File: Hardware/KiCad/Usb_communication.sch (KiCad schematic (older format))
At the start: 23 parts, among them P1 CONN_01X03, P10 CONN_01X03, P11 CONN_01X03, P12 CONN_01X03, P13 CONN_01X03, P14 CONN_01X03, P15 CONN_01X03, P16 CONN_01X03, P17 CONN_01X03, P18 CONN_01X03, P19 CONN_01X03, P2 CONN_01X03, P20 CONN_01X03, P21 CONN_01X03, P22 CONN_01X03, P23 I2C, P3 CONN_01X03, P4 CONN_01X03, P5 CONN_01X03, P6 CONN_01X03, P7 CONN_01X03, P8 CONN_01X03, P9 CONN_01X03

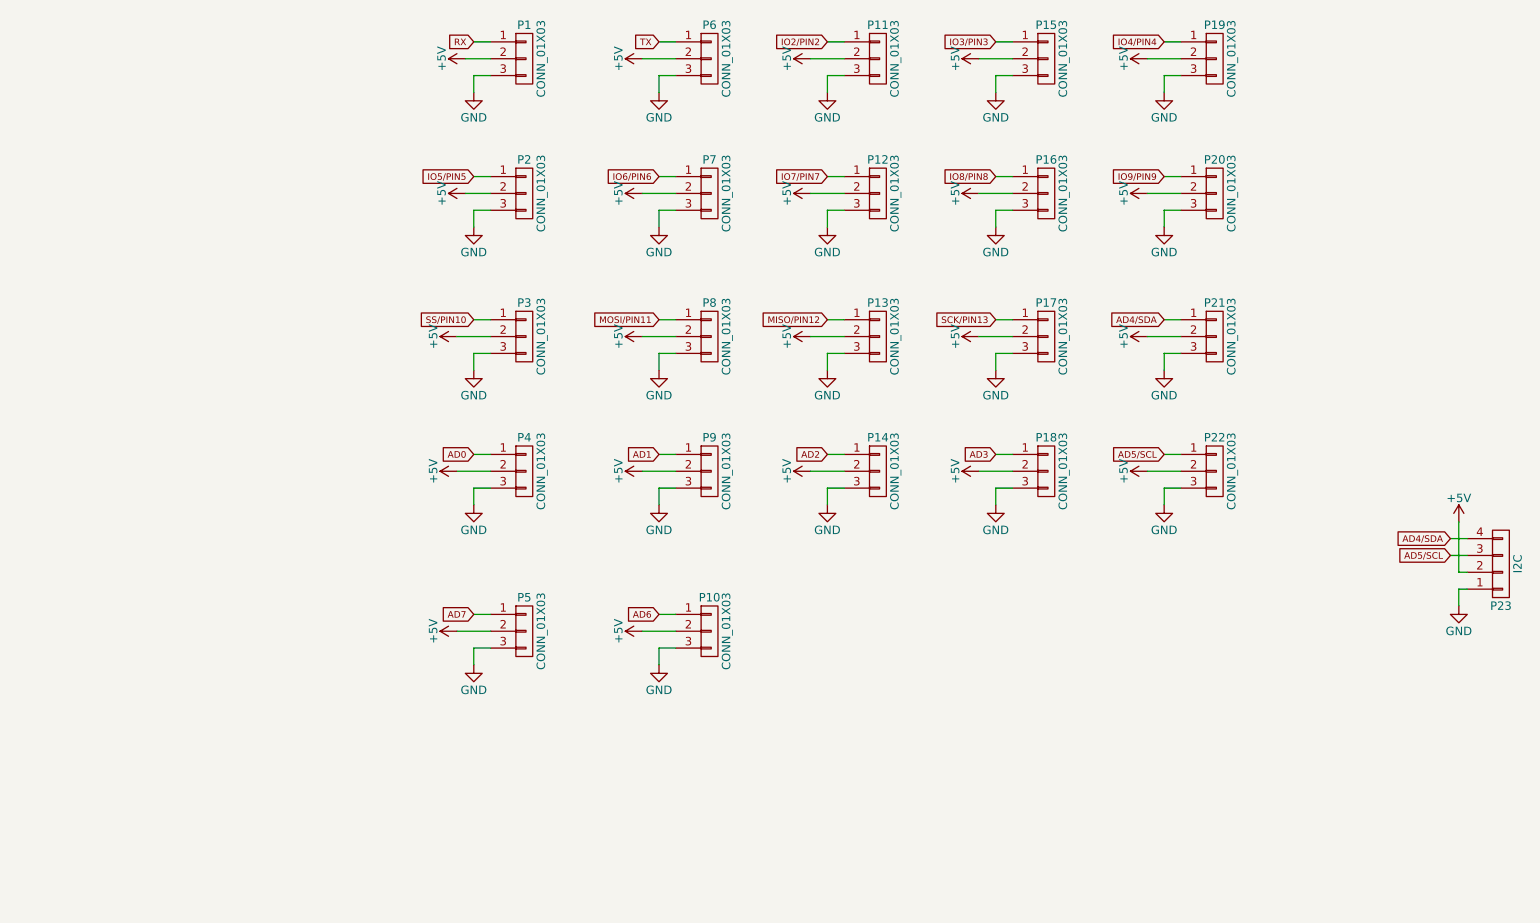
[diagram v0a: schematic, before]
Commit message: Cambiando el árbol de carpetas
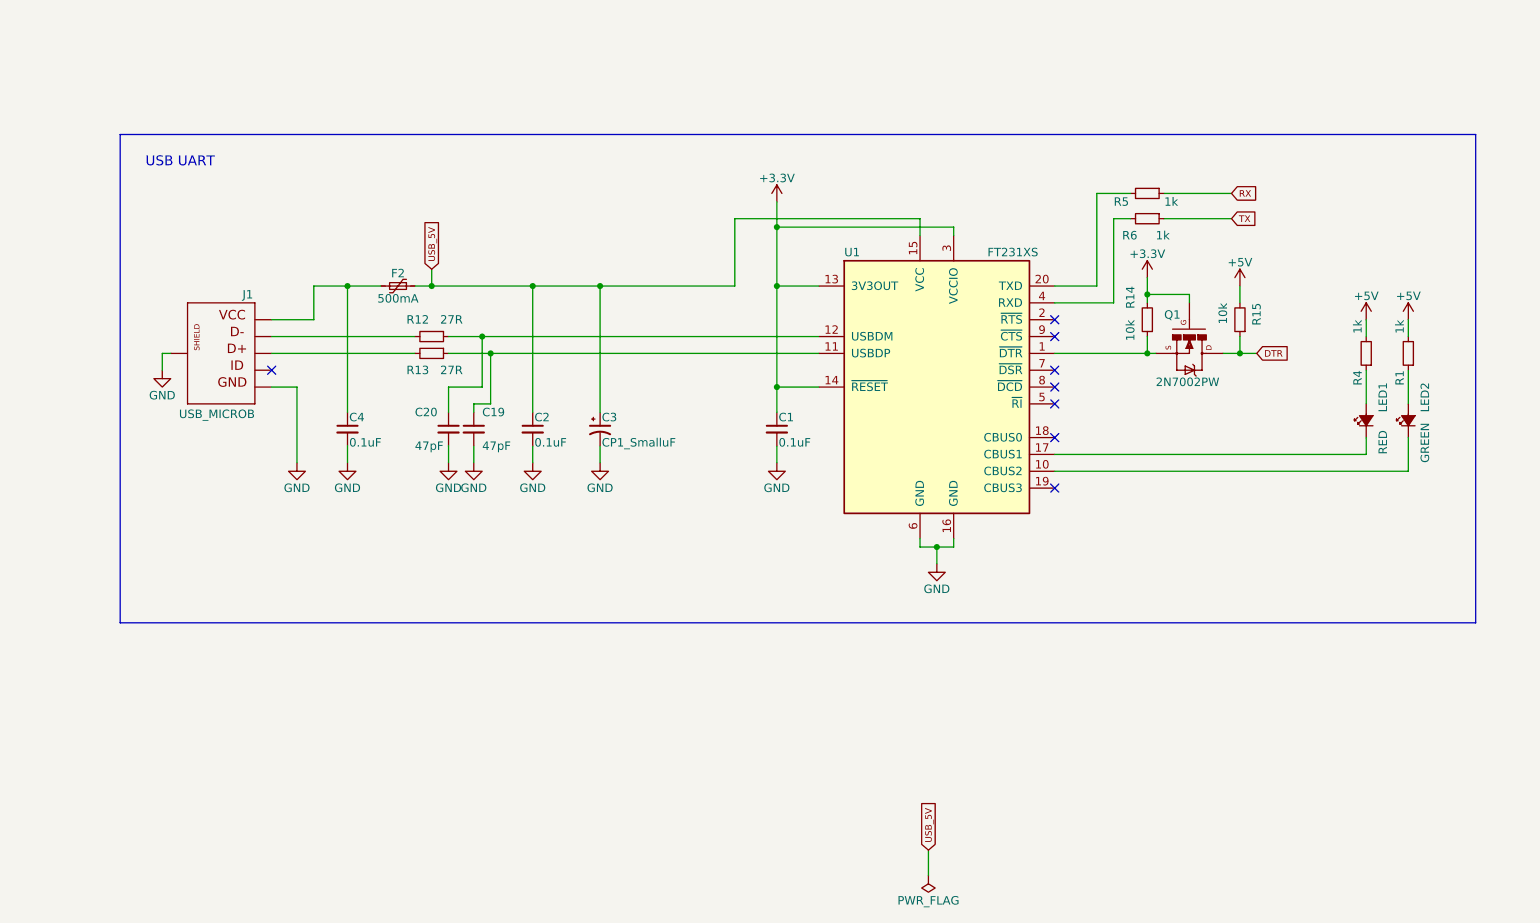
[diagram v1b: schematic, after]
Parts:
- removed P1, P10, P11, P12, P13, P14, P15, P16, P17, P18, P19, P2, P20, P21, P22, P3, P4, P5, P6, P7, P8, P9: CONN_01X03, Pin_Headers:Pin_Header_Straight_1x03_Pitch2.54mm, symbol CONN_01X03
- removed P23: I2C, Connectors_JST:JST_PH_S4B-PH-K_04x2.00mm_Angled, symbol CONN_01X04
- added C1, C2, C4: 0.1uF, lib_sch:C_0805, symbol C_Small
- added C19, C20: 47pF, lib_sch:C_0805, symbol C_Small
- added C3: CP1_SmalluF, lib_sch:CP_Tantalum_Case-A_EIA-3216-18_Reflow, symbol CP1_Small
- added F2: 500mA, lib_sch:R_1812, symbol Polyfuse_Small
- added J1: USB_MICROB, lib_sch:USB_Micro-B_Molex-105017-0001, symbol USB_MICROB_PLUGCONN-11752
- added LED1: RED, lib_sch:LED_0805, symbol LED_Small_ALT
- added LED2: GREEN, lib_sch:LED_0805, symbol LED_Small_ALT
- added Q1: 2N7002PW, lib_sch:SOT-323_SC-70, symbol MOSFET-NCHANNEL2N7002PW
- added R1, R4, R5, R6: 1k, lib_sch:R_0805, symbol R_Small
- added R12, R13: 27R, lib_sch:R_0805, symbol R_Small
- added R14, R15: 10k, lib_sch:R_0805, symbol R_Small
- added U1: FT231XS, lib_sch:SSOP-20, symbol FT231XS
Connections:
- net +5V: now also R1.2, R15.2, R4.2
- net GND: now also C1.2, C19.2, C2.2, C20.2, C3.2, C4.2, J1.5 (GND), J1.6 (SHIELD), U1.16 (GND), U1.6 (GND)
- net RX: now also R5.1
- net TX: now also R6.1
- new net: Q1.2 (S), R14.1, U1.1 (~DTR)
- new net: C4.1, F2.2, J1.1 (VCC)
- new net: C20.1, R12.1, U1.12 (USBDM)
- new net: J1.2 (D-), R12.2
- new net: LED1.1 (K), U1.17 (CBUS1)
- new net: LED1.2 (A), R4.1
- new net: J1.3 (D+), R13.2
- new net: LED2.1 (K), U1.10 (CBUS2)
- new net: C19.1, R13.1, U1.11 (USBDP)
- new net: R5.2, U1.20 (TXD)
- new net: R6.2, U1.4 (RXD)
- new net: LED2.2 (A), R1.1
- new net +3V3: C1.1, Q1.1 (G), R14.2, U1.13 (3V3OUT), U1.14 (~RESET), U1.3 (VCCIO)
- new net DTR: Q1.3 (D), R15.1
- new net USB_5V: C2.1, C3.1, F2.1, U1.15 (VCC)
- no-connect marks 0 -> 8
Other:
- note added: "USB UART\n"

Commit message: Valores cambiados
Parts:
- C1, C2, C4: value 0.1uF -> 100nF
- C3: value CP1_SmalluF -> 10nF

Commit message: preparando archivos
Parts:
- C1, C19, C2, C20, C4: symbol C_Small -> Grape:C_Small
- C3: symbol CP1_Small -> Grape:CP1_Small
- F2: symbol Polyfuse_Small -> Grape:Polyfuse_Small
- J1: symbol USB_MICROB_PLUGCONN-11752 -> Grape:USB_MICROB_PLUGCONN-11752
- LED1, LED2: symbol LED_Small_ALT -> Grape:LED_Small_ALT
- Q1: symbol MOSFET-NCHANNEL2N7002PW -> Grape:MOSFET-NCHANNEL2N7002PW
- R1, R12, R13, R14, R15, R4, R5, R6: symbol R_Small -> Grape:R_Small
- U1: symbol FT231XS -> Grape:FT231XS
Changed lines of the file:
@@
-EESchema Schematic File Version 2
-LIBS:Grape
-EELAYER 25 0
+EESchema Schematic File Version 4
+LIBS:Grape-cache
+EELAYER 26 0
 EELAYER END
 $Descr A4 11693 8268
@@
 $EndDescr
 $Comp
-L MOSFET-NCHANNEL2N7002PW Q1
+L Grape:MOSFET-NCHANNEL2N7002PW Q1
 U 1 1 5A5B8C16
 P 8050 3850
@@
 $EndComp
 $Comp
-L Polyfuse_Small F2
+L Grape:Polyfuse_Small F2
 U 1 1 5A5B942E
 P 3350 3450
@@
 $EndComp
 $Comp
-L R_Small R12
+L Grape:R_Small R12
 U 1 1 5A5B9487
 P 3550 3750
@@
 $EndComp
 $Comp
-L CP1_Small C3
+L Grape:CP1_Small C3
 U 1 1 5A5B962D
 P 4550 4300
@@
 $EndComp
 $Comp
-L LED_Small_ALT LED1
+L Grape:LED_Small_ALT LED1
 U 1 1 5A5B9670
 P 9100 4250
@@
 $EndComp
 $Comp
-L USB_MICROB_PLUGCONN-11752 J1
+L Grape:USB_MICROB_PLUGCONN-11752 J1
 U 1 1 5A5B97D7
 P 2300 3850
@@
 $EndComp
 $Comp
-L FT231XS U1
+L Grape:FT231XS U1
 U 1 1 5A5B991A
 P 6550 4050
@@
 $EndComp
 $Comp
-L GND #PWR01
+L Grape:GND #PWR01
 U 1 1 5A5B9BEF
 P 2750 4500
@@
 $EndComp
 $Comp
-L GND #PWR02
+L Grape:GND #PWR02
 U 1 1 5A5B9C19
 P 1950 3950
@@
 $EndComp
 $Comp
-L C_Small C4
+L Grape:C_Small C4
 U 1 1 5A5B9CAA
 P 3050 4300
@@
 $EndComp
 $Comp
-L GND #PWR03
+L Grape:GND #PWR03
 U 1 1 5A5B9DDB
 P 3050 4500
@@
 $EndComp
 $Comp
-L R_Small R13
+L Grape:R_Small R13
 U 1 1 5A5BA086
 P 3550 3850
@@
 NoConn ~ 2600 3950
 $Comp
-L C_Small C20
+L Grape:C_Small C20
 U 1 1 5A5BA37A
 P 3650 4300
@@
 $EndComp
 $Comp
-L C_Small C19
+L Grape:C_Small C19
 U 1 1 5A5BA405
 P 3800 4300
@@
 $EndComp
 $Comp
-L GND #PWR04
+L Grape:GND #PWR04
 U 1 1 5A5BA69F
 P 3650 4500
@@
 $EndComp
 $Comp
-L GND #PWR05
+L Grape:GND #PWR05
 U 1 1 5A5BA6CE
 P 3800 4500
@@
 $EndComp
 $Comp
-L C_Small C2
+L Grape:C_Small C2
 U 1 1 5A5BAC9D
 P 4150 4300
@@
 $EndComp
 $Comp
-L GND #PWR06
+L Grape:GND #PWR06
 U 1 1 5A5BAD72
 P 4150 4500
@@
 $EndComp
 $Comp
-L GND #PWR07
+L Grape:GND #PWR07
 U 1 1 5A5BB0A6
 P 4550 4500
@@
 	2850 3650 2850 3450
 Wire Wire Line
-	2850 3450 3250 3450
+	2850 3450 3050 3450
 Wire Wire Line
 	3050 4200 3050 3450
@@
 	3850 4050 3850 3750
 Wire Wire Line
-	3650 3750 5850 3750
-Wire Wire Line
-	3650 3850 5850 3850
+	3650 3750 3850 3750
+Wire Wire Line
+	3650 3850 3900 3850
 Wire Wire Line
 	3900 3850 3900 4150
@@
 	4150 3450 4150 4200
 Wire Wire Line
-	3450 3450 5350 3450
+	3450 3450 3550 3450
 Wire Wire Line
 	3550 3450 3550 3350
@@
 Connection ~ 4550 3450
 $Comp
-L C_Small C1
+L Grape:C_Small C1
 U 1 1 5A5BB3AE
 P 5600 4300
@@
 $EndComp
 $Comp
-L GND #PWR08
+L Grape:GND #PWR08
 U 1 1 5A5BB45B
 P 5600 4500
@@
 	5600 4400 5600 4500
 Wire Wire Line
-	5600 2950 5600 4200
+	5600 2950 5600 3100
 Wire Wire Line
 	5600 4050 5850 4050
@@
 Connection ~ 5600 3100
 $Comp
-L +3.3V #PWR09
+L Grape:+3.3V #PWR09
 U 1 1 5A5BB5E3
 P 5600 2950
@@
 $EndComp
 $Comp
-L GND #PWR010
+L Grape:GND #PWR010
 U 1 1 5A5BB73F
 P 6550 5100
@@
 	6450 4950 6450 5000
 Wire Wire Line
-	6450 5000 6650 5000
+	6450 5000 6550 5000
 Wire Wire Line
 	6550 5000 6550 5100
@@
 NoConn ~ 7250 4150
 $Comp
-L R_Small R5
+L Grape:R_Small R5
 U 1 1 5A5BBBAB
 P 7800 2900
@@
 $EndComp
 $Comp
-L R_Small R6
+L Grape:R_Small R6
 U 1 1 5A5BBD20
 P 7800 3050
@@
 TX
 $Comp
-L LED_Small_ALT LED2
+L Grape:LED_Small_ALT LED2
 U 1 1 5A5BC688
 P 9350 4250
@@
 	9350 4550 7250 4550
 $Comp
-L R_Small R4
+L Grape:R_Small R4
 U 1 1 5A5BC7D4
 P 9100 3850
@@
 $EndComp
 $Comp
-L R_Small R1
+L Grape:R_Small R1
 U 1 1 5A5BC864
 P 9350 3850
@@
 	9350 3950 9350 4150
 $Comp
-L +5V #PWR011
+L Grape:+5V #PWR011
 U 1 1 5A5BCDBB
 P 9100 3650
@@
 $EndComp
 $Comp
-L +5V #PWR012
+L Grape:+5V #PWR012
 U 1 1 5A5BCE2C
 P 9350 3650
@@
 	9100 3650 9100 3750
 Wire Wire Line
-	7250 3850 7850 3850
-$Comp
-L R_Small R14
+	7250 3850 7800 3850
+$Comp
+L Grape:R_Small R14
 U 1 1 5A5BD495
 P 7800 3650
@@
 $EndComp
 $Comp
-L R_Small R15
+L Grape:R_Small R15
 U 1 1 5A5BD4FF
 P 8350 3650
@@
 Connection ~ 7800 3850
 Wire Wire Line
-	8250 3850 8450 3850
+	8250 3850 8350 3850
 Wire Wire Line
 	8350 3850 8350 3750
 Connection ~ 8350 3850
 $Comp
-L +5V #PWR013
+L Grape:+5V #PWR013
 U 1 1 5A5BD7FA
 P 8350 3450
@@
 	8350 3450 8350 3550
 $Comp
-L +3.3V #PWR014
+L Grape:+3.3V #PWR014
 U 1 1 5A5BDBB8
 P 7800 3400
@@
 $EndComp
 Wire Wire Line
-	7800 3400 7800 3550
+	7800 3400 7800 3500
 Wire Wire Line
 	7800 3500 8050 3500
@@
 $Bitmap
 Pos 10850 6200
-Scale 0,950000
+Scale 0.000000
 Data
 89 50 4E 47 0D 0A 1A 0A 00 00 00 0D 49 48 44 52 00 00 00 C1 00 00 00 8F 08 06 00 00 00 43 10 BF
@@
 $Bitmap
 Pos 7250 6700
-Scale 0,950000
+Scale 0.000000
 Data
 89 50 4E 47 0D 0A 1A 0A 00 00 00 0D 49 48 44 52 00 00 00 91 00 00 00 36 08 06 00 00 00 C7 C1 7B
@@
 USB_5V
 $Comp
-L PWR_FLAG #FLG015
+L Grape:PWR_FLAG #FLG015
 U 1 1 5A5DCFF9
 P 6500 6950
@@
 Text Notes 1850 2750 0    59   ~ 0
 USB UART\n
+Wire Wire Line
+	3050 3450 3250 3450
+Wire Wire Line
+	3850 3750 5850 3750
+Wire Wire Line
+	3900 3850 5850 3850
+Wire Wire Line
+	3550 3450 4150 3450
+Wire Wire Line
+	4150 3450 4550 3450
+Wire Wire Line
+	4550 3450 5350 3450
+Wire Wire Line
+	5600 4050 5600 4200
+Wire Wire Line
+	5600 3450 5600 4050
+Wire Wire Line
+	5600 3100 5600 3450
+Wire Wire Line
+	6550 5000 6650 5000
+Wire Wire Line
+	7800 3850 7850 3850
+Wire Wire Line
+	8350 3850 8450 3850
+Wire Wire Line
+	7800 3500 7800 3550
 $EndSCHEMATC

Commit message: Prueba de guardado
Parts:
- removed J1: USB_MICROB, lib_sch:USB_Micro-B_Molex-105017-0001, symbol Grape:USB_MICROB_PLUGCONN-11752
- added R? (x2): 5k1, lib_sch:R_0805, symbol Grape:R_Small
- added USB?: HRO-TYPE-C-31-M-12, symbol Type-C:HRO-TYPE-C-31-M-12
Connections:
- wire segments 78 -> 95
- no-connect marks 8 -> 11
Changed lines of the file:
@@
 EESchema Schematic File Version 4
-LIBS:Grape-cache
-EELAYER 26 0
+EELAYER 30 0
 EELAYER END
 $Descr A4 11693 8268
@@
 $EndComp
 $Comp
-L Grape:USB_MICROB_PLUGCONN-11752 J1
-U 1 1 5A5B97D7
-P 2300 3850
-F 0 "J1" H 2110 4170 50  0000 L BNN
-F 1 "USB_MICROB" H 2100 3460 50  0000 L BNN
-F 2 "lib_sch:USB_Micro-B_Molex-105017-0001" H 2330 4000 20  0001 C CNN
-F 3 "" H 2300 3850 60  0000 C CNN
-	1    2300 3850
-	-1   0    0    -1
-$EndComp
-$Comp
 L Grape:FT231XS U1
 U 1 1 5A5B991A
@@
 F 3 "" H 2750 4500 60  0000 C CNN
 	1    2750 4500
-	1    0    0    -1
-$EndComp
-$Comp
-L Grape:GND #PWR02
-U 1 1 5A5B9C19
-P 1950 3950
-F 0 "#PWR02" H 1950 3700 50  0001 C CNN
-F 1 "GND" H 1950 3800 50  0000 C CNN
-F 2 "" H 1950 3950 60  0000 C CNN
-F 3 "" H 1950 3950 60  0000 C CNN
-	1    1950 3950
 	1    0    0    -1
 $EndComp
@@
 $EndComp
 Wire Wire Line
-	1950 3950 1950 3850
-Wire Wire Line
-	1950 3850 2000 3850
-Wire Wire Line
 	2600 4050 2750 4050
 Wire Wire Line
@@
 $Bitmap
 Pos 10850 6200
-Scale 0.000000
+Scale 1.000000
 Data
 89 50 4E 47 0D 0A 1A 0A 00 00 00 0D 49 48 44 52 00 00 00 C1 00 00 00 8F 08 06 00 00 00 43 10 BF
@@
 $Bitmap
 Pos 7250 6700
-Scale 0.000000
+Scale 1.000000
 Data
 89 50 4E 47 0D 0A 1A 0A 00 00 00 0D 49 48 44 52 00 00 00 91 00 00 00 36 08 06 00 00 00 C7 C1 7B
@@
 Wire Wire Line
 	7800 3500 7800 3550
+$Comp
+L Type-C:HRO-TYPE-C-31-M-12 USB?
+U 1 1 5FB09824
+P 1850 3900
+F 0 "USB?" H 1683 4697 60  0000 C CNN
+F 1 "HRO-TYPE-C-31-M-12" H 1683 4591 60  0000 C CNN
+F 2 "" H 1850 3900 60  0001 C CNN
+F 3 "" H 1850 3900 60  0001 C CNN
+	1    1850 3900
+	1    0    0    -1
+$EndComp
+$Comp
+L Grape:GND #PWR?
+U 1 1 5FB0C5BE
+P 2100 4650
+F 0 "#PWR?" H 2100 4400 50  0001 C CNN
+F 1 "GND" H 2100 4500 50  0000 C CNN
+F 2 "" H 2100 4650 60  0000 C CNN
+F 3 "" H 2100 4650 60  0000 C CNN
+	1    2100 4650
+	1    0    0    -1
+$EndComp
+Wire Wire Line
+	1950 4450 2100 4450
+Wire Wire Line
+	2100 4450 2100 4650
+Wire Wire Line
+	2100 4450 2100 3350
+Wire Wire Line
+	2100 3350 1950 3350
+Connection ~ 2100 4450
+Wire Wire Line
+	1950 3450 2250 3450
+Wire Wire Line
+	2250 3450 2250 3300
+Wire Wire Line
+	1950 4350 2250 4350
+Wire Wire Line
+	2250 4350 2250 3450
+Connection ~ 2250 3450
+Wire Wire Line
+	1950 3850 2450 3850
+Wire Wire Line
+	1950 4050 2450 4050
+Wire Wire Line
+	2450 4050 2450 3950
+Wire Wire Line
+	2450 3950 2500 3950
+Connection ~ 2450 3950
+Wire Wire Line
+	2450 3950 2450 3850
+Wire Wire Line
+	1950 3950 2150 3950
+Wire Wire Line
+	2150 3950 2150 3750
+Wire Wire Line
+	2150 3750 1950 3750
+Wire Wire Line
+	2150 3750 2500 3750
+Connection ~ 2150 3750
+Wire Wire Line
+	1950 3650 2500 3650
+Wire Wire Line
+	1950 4250 2500 4250
+NoConn ~ 1950 4550
+NoConn ~ 1950 4150
+NoConn ~ 1950 3550
+$Comp
+L Grape:R_Small R?
+U 1 1 5FB3A3EB
+P 2500 4950
+F 0 "R?" V 2600 4800 50  0000 L CNN
+F 1 "5k1" V 2600 5000 50  0000 L CNN
+F 2 "lib_sch:R_0805" H 2500 4950 50  0001 C CNN
+F 3 "" H 2500 4950 50  0001 C CNN
+	1    2500 4950
+	0    1    1    0
+$EndComp
+$Comp
+L Grape:R_Small R?
+U 1 1 5FB3A92F
+P 2500 5200
+F 0 "R?" V 2600 5050 50  0000 L CNN
+F 1 "5k1" V 2600 5250 50  0000 L CNN
+F 2 "lib_sch:R_0805" H 2500 5200 50  0001 C CNN
+F 3 "" H 2500 5200 50  0001 C CNN
+	1    2500 5200
+	0    1    1    0
+$EndComp
 $EndSCHEMATC

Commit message: Conector y CH340C implementado
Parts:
- removed C19, C20: 47pF, lib_sch:C_0805, symbol Grape:C_Small
- removed Q1: 2N7002PW, lib_sch:SOT-323_SC-70, symbol Grape:MOSFET-NCHANNEL2N7002PW
- removed R12, R13: 27R, lib_sch:R_0805, symbol Grape:R_Small
- removed R14, R15: 10k, lib_sch:R_0805, symbol Grape:R_Small
- removed R5, R6: 1k, lib_sch:R_0805, symbol Grape:R_Small
- removed R?: 5k1, lib_sch:R_0805, symbol Grape:R_Small
- removed U1: FT231XS, lib_sch:SSOP-20, symbol Grape:FT231XS
- added C?: 100nF, lib_sch:C_0805, symbol Grape:C_Small
- added R?: 5k1, lib_sch:R_0805, symbol Grape:R_Small
- added U?: CH340C, Package_SO:SOIC-16_3.9x9.9mm_P1.27mm, symbol Interface_USB:CH340C
- C1: value 100nF -> 10nF
- R1, R4: value 1k -> 4k7
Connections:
- net labels added: VCC
- net labels removed: +3.3V, +5V
- wire segments 95 -> 56
- no-connect marks 11 -> 9
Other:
- moved on the sheet: C1, C2, C3, C4, F2, LED1, LED2, R1, R4, R?, USB?

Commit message: Esquema terminado
Falta comprobar
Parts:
- F2: value 500mA -> 2A
- gave numbers to parts that had none: 5
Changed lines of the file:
@@
 P 4650 3600
 F 0 "F2" V 4575 3600 50  0000 C CNN
-F 1 "500mA" V 4725 3600 50  0000 C CNN
+F 1 "2A" V 4725 3600 50  0000 C CNN
 F 2 "lib_sch:R_1812" H 4700 3400 50  0001 L CNN
 F 3 "" H 4650 3600 50  0001 C CNN
@@
 P 7100 3400
 F 0 "LED1" H 7150 3300 50  0000 L CNN
-F 1 "RED" H 6900 3300 50  0000 L CNN
+F 1 "RED" H 7000 3300 50  0000 L CNN
 F 2 "lib_sch:LED_0805" V 7100 3400 50  0001 C CNN
 F 3 "" V 7100 3400 50  0001 C CNN
@@
 P 7350 3400
 F 0 "LED2" H 7400 3300 50  0000 L CNN
-F 1 "GREEN" H 7100 3300 50  0000 L CNN
+F 1 "GREEN" H 7150 3300 50  0000 L CNN
 F 2 "lib_sch:LED_0805" V 7350 3400 50  0001 C CNN
 F 3 "" V 7350 3400 50  0001 C CNN
@@
 	4350 3600 4550 3600
 $Comp
-L Type-C:HRO-TYPE-C-31-M-12 USB?
+L Type-C:HRO-TYPE-C-31-M-12 USB1
 U 1 1 5FB09824
 P 3150 4050
-F 0 "USB?" H 2983 4847 60  0000 C CNN
+F 0 "USB1" H 2983 4847 60  0000 C CNN
 F 1 "HRO-TYPE-C-31-M-12" H 2983 4741 60  0000 C CNN
 F 2 "" H 3150 4050 60  0001 C CNN
@@
 $EndComp
 $Comp
-L Grape:GND #PWR?
+L Grape:GND #PWR01
 U 1 1 5FB0C5BE
 P 3400 5100
-F 0 "#PWR?" H 3400 4850 50  0001 C CNN
+F 0 "#PWR01" H 3400 4850 50  0001 C CNN
 F 1 "GND" H 3400 4950 50  0000 C CNN
 F 2 "" H 3400 5100 60  0000 C CNN
@@
 NoConn ~ 3250 3700
 $Comp
-L Grape:R_Small R?
+L Grape:R_Small R5
 U 1 1 5FB3A3EB
 P 3650 4900
-F 0 "R?" V 3750 4850 50  0000 L CNN
+F 0 "R5" V 3750 4850 50  0000 L CNN
 F 1 "5k1" V 3750 4950 50  0000 L CNN
 F 2 "lib_sch:R_0805" H 3650 4900 50  0001 C CNN
@@
 $EndComp
 $Comp
-L Grape:R_Small R?
+L Grape:R_Small R6
 U 1 1 5FB96FA9
 P 3800 4900
-F 0 "R?" H 3741 4854 50  0000 R CNN
+F 0 "R6" H 3741 4854 50  0000 R CNN
 F 1 "5k1" H 3741 4945 50  0000 R CNN
 F 2 "lib_sch:R_0805" H 3800 4900 50  0001 C CNN
@@
 $EndComp
 $Comp
-L Grape:GND #PWR?
+L Grape:GND #PWR02
 U 1 1 5FB978E2
 P 3650 5100
-F 0 "#PWR?" H 3650 4850 50  0001 C CNN
+F 0 "#PWR02" H 3650 4850 50  0001 C CNN
 F 1 "GND" H 3650 4950 50  0000 C CNN
 F 2 "" H 3650 5100 60  0000 C CNN
@@
 	3650 5100 3650 5000
 $Comp
-L Grape:GND #PWR?
+L Grape:GND #PWR04
 U 1 1 5FB99D36
 P 3800 5100
-F 0 "#PWR?" H 3800 4850 50  0001 C CNN
+F 0 "#PWR04" H 3800 4850 50  0001 C CNN
 F 1 "GND" H 3800 4950 50  0000 C CNN
 F 2 "" H 3800 5100 60  0000 C CNN
@@
 DTR
 $Comp
-L Interface_USB:CH340C U?
+L Interface_USB:CH340C U1
 U 1 1 5FC1CCA8
 P 6500 4000
-F 0 "U?" H 6250 4550 50  0000 C CNN
+F 0 "U1" H 6250 4550 50  0000 C CNN
 F 1 "CH340C" H 6750 3450 50  0000 C CNN
 F 2 "Package_SO:SOIC-16_3.9x9.9mm_P1.27mm" H 6550 3450 50  0001 L CNN
@@
 NoConn ~ 6100 3700
 $Comp
-L Grape:GND #PWR?
+L Grape:GND #PWR09
 U 1 1 5FC3174C
 P 6500 4700
-F 0 "#PWR?" H 6500 4450 50  0001 C CNN
+F 0 "#PWR09" H 6500 4450 50  0001 C CNN
 F 1 "GND" H 6500 4550 50  0000 C CNN
 F 2 "" H 6500 4700 60  0000 C CNN
@@
 	6900 3600 7100 3600
 $Comp
-L power:VCC #PWR?
+L power:VCC #PWR05
 U 1 1 5FC5A325
 P 6500 2850
-F 0 "#PWR?" H 6500 2700 50  0001 C CNN
+F 0 "#PWR05" H 6500 2700 50  0001 C CNN
 F 1 "VCC" H 6517 3023 50  0000 C CNN
 F 2 "" H 6500 2850 50  0001 C CNN
@@
 	6500 3250 6500 3400
 $Comp
-L power:VCC #PWR?
+L power:VCC #PWR011
 U 1 1 5FC5C118
 P 7100 2850
-F 0 "#PWR?" H 7100 2700 50  0001 C CNN
+F 0 "#PWR011" H 7100 2700 50  0001 C CNN
 F 1 "VCC" H 7117 3023 50  0000 C CNN
 F 2 "" H 7100 2850 50  0001 C CNN
@@
 $EndComp
 $Comp
-L power:VCC #PWR?
+L power:VCC #PWR012
 U 1 1 5FC5D1A8
 P 7350 2850
-F 0 "#PWR?" H 7350 2700 50  0001 C CNN
+F 0 "#PWR012" H 7350 2700 50  0001 C CNN
 F 1 "VCC" H 7367 3023 50  0000 C CNN
 F 2 "" H 7350 2850 50  0001 C CNN
@@
 	7350 2850 7350 2900
 $Comp
-L Grape:C_Small C?
+L Grape:C_Small C17
 U 1 1 5FC81449
 P 6650 3250
-F 0 "C?" H 6660 3320 50  0000 L CNN
+F 0 "C17" H 6660 3320 50  0000 L CNN
 F 1 "100nF" H 6660 3170 50  0000 L CNN
 F 2 "lib_sch:C_0805" H 6650 3250 50  0001 C CNN
@@
 $EndComp
 $Comp
-L Grape:GND #PWR?
+L Grape:GND #PWR010
 U 1 1 5FC81CEB
 P 6800 3250
-F 0 "#PWR?" H 6800 3000 50  0001 C CNN
+F 0 "#PWR010" H 6800 3000 50  0001 C CNN
 F 1 "GND" H 6800 3100 50  0000 C CNN
 F 2 "" H 6800 3250 60  0000 C CNN
@@
 	6500 2850 6500 3250
 Connection ~ 6500 3250
+$Comp
+L power:VCC #PWR?
+U 1 1 5FC8A642
+P 6100 6750
+F 0 "#PWR?" H 6100 6600 50  0001 C CNN
+F 1 "VCC" H 6117 6923 50  0000 C CNN
+F 2 "" H 6100 6750 50  0001 C CNN
+F 3 "" H 6100 6750 50  0001 C CNN
+	1    6100 6750
+	1    0    0    -1
+$EndComp
+$Comp
+L Grape:PWR_FLAG #FLG?
+U 1 1 5FC8BC09
+P 6100 6950
+F 0 "#FLG?" H 6100 7025 50  0001 C CNN
+F 1 "PWR_FLAG" H 6100 7100 50  0000 C CNN
+F 2 "" H 6100 6950 50  0001 C CNN
+F 3 "" H 6100 6950 50  0001 C CNN
+	1    6100 6950
+	-1   0    0    1
+$EndComp
+Wire Wire Line
+	6100 6950 6100 6750
 $EndSCHEMATC
